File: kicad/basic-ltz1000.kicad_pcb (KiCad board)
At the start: 2 copper layers, 49.5 x 49.5 mm, 33 parts, among them P1 CONN_1X1, P2 CONN_1X1, P3 CONN_1X1, P4 CONN_1X1, Q1 2N3904, U1 LTZ1000A, U2 LT1013

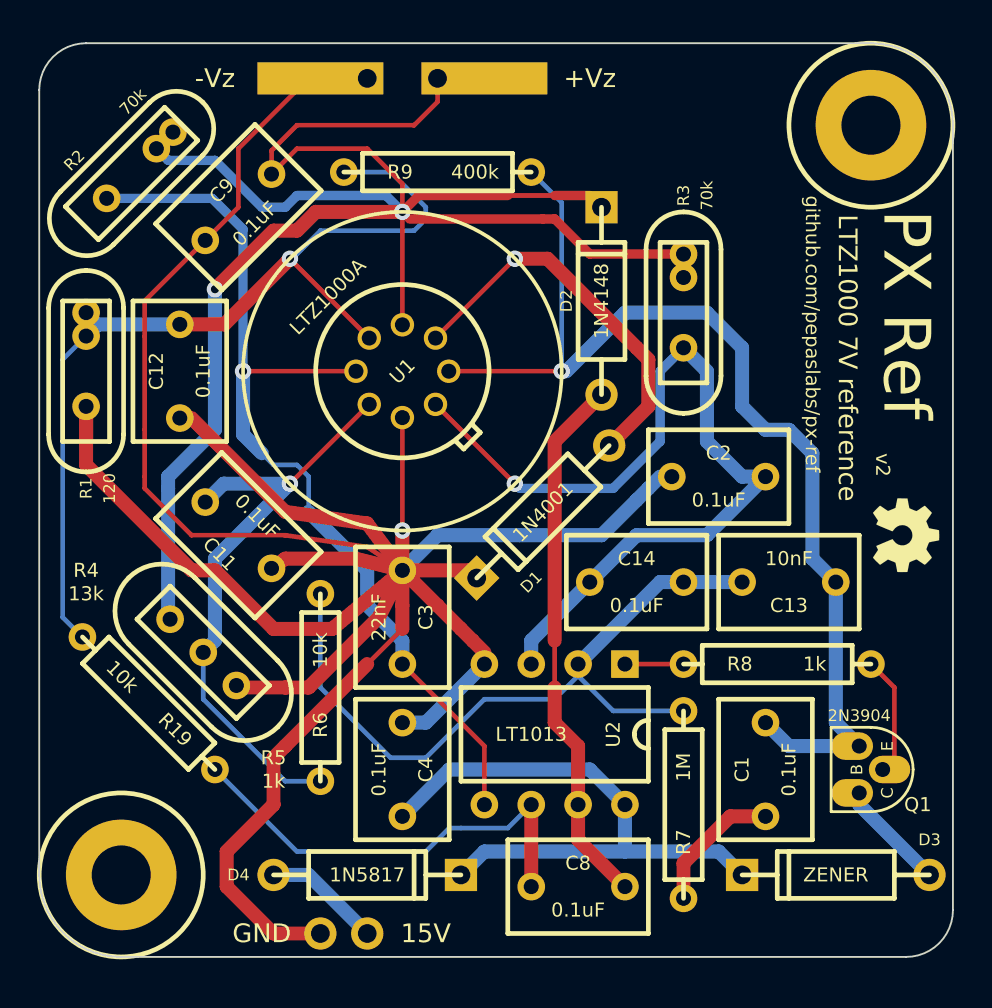
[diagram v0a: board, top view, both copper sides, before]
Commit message: Updating footprints for caps and diodes
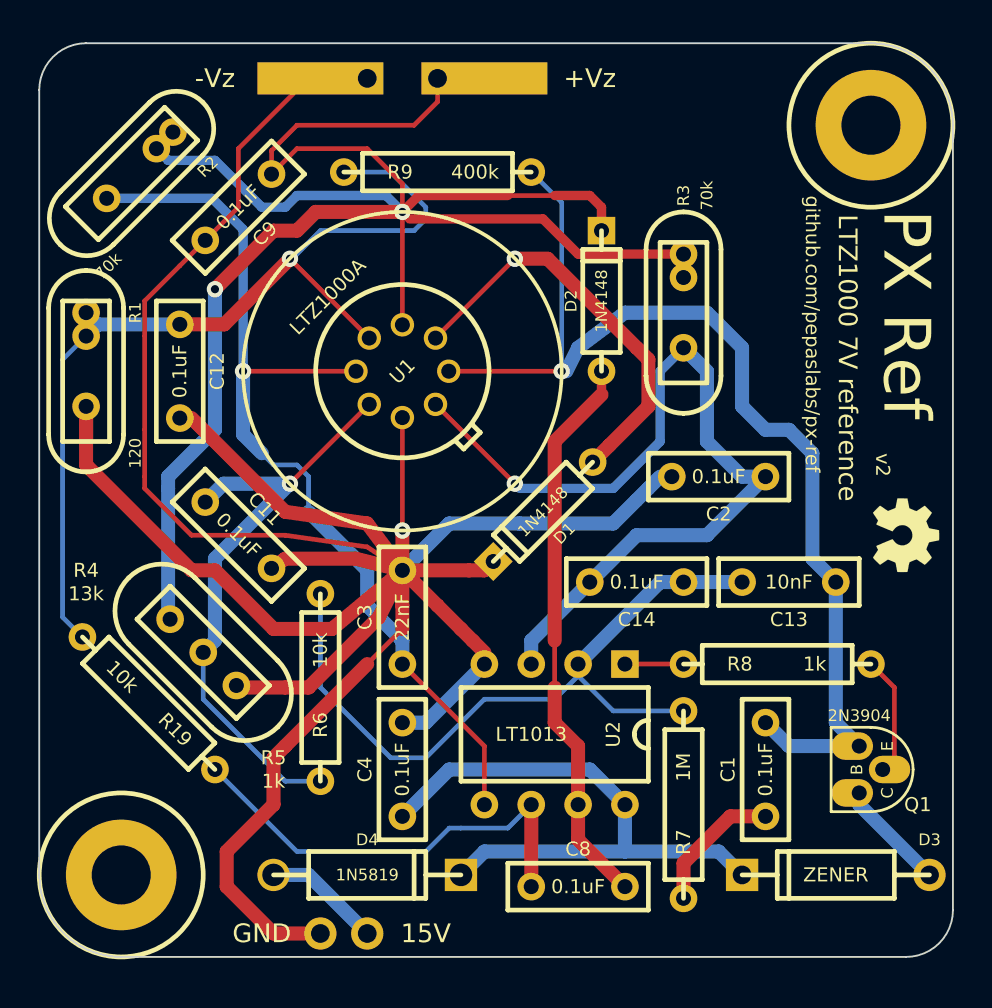
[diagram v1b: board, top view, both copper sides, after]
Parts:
- C1, C11, C12, C13, C14, C2, C3, C4, C8, C9: footprint BOXCAP_02_03_02_059A -> BOXCAP_01_03_02_059A
- D1: value 1N4001 -> 1N4148; footprint DIODE_1A_069A_PL -> DIODE_SS_059A_PL
- D2: footprint DIODE_1A_069A_PL -> DIODE_SS_059A_PL
- D4: value 1N5817 -> 1N5819
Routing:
- net Vz+ Sense: track 105.1 -> 106.3 mm
- net N-0000015: track 29.3 -> 30.6 mm
- net N-0000010: track 21.1 -> 22.4 mm
- net Vz- Sense: track 180.8 -> 181.8 mm

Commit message: reroute WIP
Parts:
- added C15: 0.1uF, BOXCAP_01_03_02_059A, F.Cu at (223.5, 111.1)
- added P5: CONN_1X1, 1pin_040_069, F.Cu at (217.8, 93.3)
- moved C3 6.63 mm to (215.9, 102.2)
- moved C4 2.29 mm to (219.1, 102.2)
- moved C8 1.42 mm to (226.1, 111.1), turned to 270 degrees
- moved D4 1.27 mm to (214.6, 109.9)
- moved G*** 0.64 mm to (245.1, 92.1)
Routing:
- net N-000005: track 51.8 -> 64.3 mm
- net Vz- Sense: track 181.8 -> 187.3 mm
- net N-0000014: track 30.6 -> 33.2 mm
- net N-000003: track 6.40 -> 7.67 mm
- net 15V: track 48.1 -> 47.0 mm
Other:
- board text added: "v2.1"
- board text removed: "v2"

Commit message: WIP
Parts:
- D3: footprint DIODE_1A_069A_PL -> DIODE_SS_059A_PL
- moved D2 23.9 mm to (233.0, 102.2)
- moved D4 10.5 mm to (224.8, 112.4)
- moved C9 9.94 mm to (217.8, 69.2), turned to 180 degrees
- moved R6 8.64 mm to (210.8, 96.5), turned to 0 degrees
- moved C13 8.28 mm to (243.2, 101.0)
- moved Q1 7.10 mm to (243.8, 109.9)
- moved C2 6.75 mm to (229.9, 92.7)
- moved R7 6.35 mm to (238.1, 107.3)
- moved C1 5.75 mm to (243.2, 103.5), turned to 0 degrees
- moved R3 5.75 mm to (232.4, 83.2)
- moved D3 5.12 mm to (236.9, 112.4)
- moved P1 5.08 mm to (210.8, 113.0)
- moved P4 5.08 mm to (208.3, 113.0)
- moved C15 4.58 mm to (219.7, 108.6), turned to 180 degrees
- moved C14 3.70 mm to (227.3, 95.9)
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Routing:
- net Vz- Sense: track 187.3 -> 162.0 mm
- net 15V: track 47.0 -> 22.3 mm
- net N-0000014: track 33.2 -> 10.7 mm
- net Vz+ Sense: track 106.3 -> 127.2 mm, vias 2 -> 1
- net N-000004: track 47.9 -> 32.3 mm
- net N-0000013: track 41.0 -> 26.3 mm
- net N-0000010: track 32.9 -> 22.7 mm
- net N-0000015: track 51.5 -> 42.1 mm
- net N-000005: track 64.3 -> 55.3 mm
- net H+: track 60.2 -> 69.1 mm
- net N-0000012: track 3.17 -> 8.65 mm
- net N-0000011: track 6.50 -> 11.3 mm
- net N-000009: track 22.4 -> 18.6 mm
- net N-000007: track 6.02 -> 3.18 mm
- net N-0000016: track 7.40 -> 4.58 mm
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
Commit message: v2.1 gerbers
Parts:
- removed C9: 0.1uF, BOXCAP_01_03_02_059A
- removed the H*** at (202.6, 109.9)
- removed P3: CONN_1X1, 1pin_040_069_strip_2_PL
- added H1: HOLE, hole_M3, F.Cu at (202.6, 109.9)
- added P6: CONN_2X1, SIL-2, F.Cu at (199.4, 104.1)
- P2: footprint 1pin_040_069_strip_2_PL -> 1pin_040_069
- R1, R2, R3: footprint R_BOX_PL -> R_BOX_HERMETIC_PL
- moved R19 3.42 mm to (206.4, 101.0)
- moved P2 2.84 mm to (217.8, 68.6), turned to 0 degrees
- moved R1 2.29 mm to (201.9, 82.5)
- moved R2 2.29 mm to (206.4, 71.8)
- moved R3 1.91 mm to (232.4, 85.1)
- moved R45 0.90 mm to (205.7, 94.6)
- moved C11 0.90 mm to (209.6, 90.8)
- moved C12 0.63 mm to (206.4, 82.5)
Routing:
- net Vz- Sense: track 162.0 -> 137.2 mm
- net Vz+ Sense: track 127.2 -> 113.9 mm
- net CHASSIS: track 0.00 -> 6.54 mm
- net N-000008: track 23.3 -> 26.4 mm
- net N-000007: track 55.3 -> 52.9 mm
- net N-0000016: track 42.1 -> 43.7 mm
- net N-0000011: track 22.7 -> 21.7 mm
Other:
- board text added: "CHASSIS"

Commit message: v2.2 gerbers
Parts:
- added C30: 0.1uF, BOXCAP_01_03_02_059A, F.Cu at (241.9, 78.7)
- added C31: 10nF, BOXCAP_01_03_02_059A, F.Cu at (241.9, 81.3)
- added C33: 0.1uF, BOXCAP_01_03_02_059A, F.Cu at (241.9, 93.3)
- added P3: CONN_1X1, 1pin_040_069, F.Cu at (236.2, 91.4)
- added R30: 10k, R_AXIAL_0W25_059A_PL, F.Cu at (228.6, 73.7)
- added R31: 10k, R_AXIAL_0W25_059A_PL, F.Cu at (246.4, 76.2)
- added R32: 22R, R_AXIAL_0W25_059A_PL, F.Cu at (236.2, 78.7)
- added U30: LTC2057, SO-8, F.Cu at (241.9, 87.6)
- moved G*** 50.9 mm to (200.7, 67.3), turned to 0 degrees
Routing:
- net Vz- Sense: track 137.2 -> 208.4 mm, vias 1 -> 2
- net 15V: track 22.3 -> 56.5 mm
- net N-000008: track 0.00 -> 16.3 mm
- net N-000007: track 0.00 -> 11.9 mm
- net Vz+ Sense: track 113.9 -> 125.3 mm
- net N-0000011: track 0.00 -> 10.1 mm
- net Vz+ Buf: track 0.00 -> 2.54 mm
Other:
- board text added: "BUF"
- board text added: "v2.2"
- board text removed: "v2.1"

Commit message: v2.2 revisions
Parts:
- removed the G*** at (200.7, 67.3)
- added G***: OSHW-logo_silkscreen-front_5mm, OSHW-logo_silkscreen-front_5mm, F.Cu at (201.3, 67.7)
- moved C33 0.63 mm to (242.6, 93.3)
- moved U30 0.63 mm to (242.6, 87.6)
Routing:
- net Vz- Sense: track 208.4 -> 243.8 mm, vias 2 -> 3
- net 15V: track 56.5 -> 60.1 mm
- net H+: track 69.1 -> 66.9 mm
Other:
- outline, holes or cut-outs redrawn

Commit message: fixing output buffer, adding copper zones
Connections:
- C31 pad 2: N-000008 -> N-0000010
- R31 pad 2: N-000008 -> Vz+ Buf
- R32 pad 1: N-000008 -> N-0000010
- U30 pad 6: N-000008 -> N-0000010
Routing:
- net N-000008: track 16.8 -> 0.00 mm
- net N-0000010: track 0.00 -> 14.2 mm
- net Vz+ Buf: track 2.54 -> 16.2 mm
- added copper zone on B.Cu, net (none)
- added copper zone on F.Cu, net (none)

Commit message: 2.2b
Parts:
- removed R45: 1k / 13k, R_BOX_DIVIDER_PL
- added R4: 13k, R_BOX_PL, F.Cu at (205.7, 93.3)
- added R5: 1k, R_BOX_PL, F.Cu at (203.8, 95.2)
- moved R19 12.1 mm to (214.6, 109.9)
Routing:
- net N-0000014: track 26.4 -> 14.4 mm
- net N-0000021: track 43.7 -> 55.3 mm
- net N-000008: track 21.7 -> 26.1 mm
- net Vz- Sense: track 243.8 -> 245.9 mm
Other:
- board text added: "v2.2b"
- board text removed: "13k"
- board text removed: "1k"
- board text removed: "R4"
- board text removed: "R5"
- board text removed: "v2.2"
